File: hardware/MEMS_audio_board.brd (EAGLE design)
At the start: 43.2 x 25.4 mm, 20 parts, among them J1 SJ-2524-SMT, J2 USBSMD, U1 LMV793MF, U2 MIC5365-3.3YD5

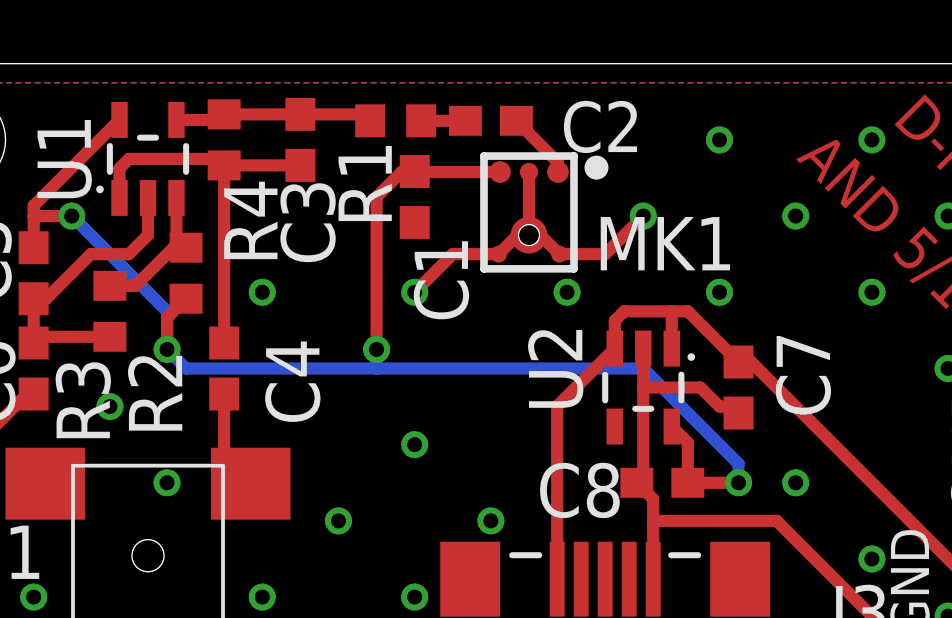
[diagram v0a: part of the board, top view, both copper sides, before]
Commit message: corrected flipped mic layout
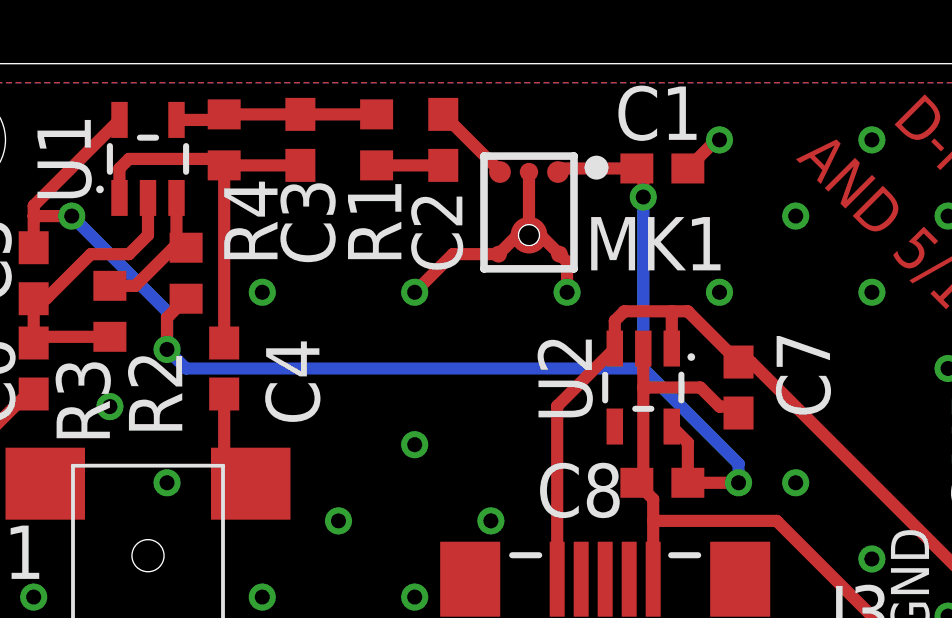
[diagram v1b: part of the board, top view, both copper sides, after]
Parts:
- moved C1 8.31 mm to (26.0, 21.9), turned to 0 degrees
- moved C2 1.71 mm to (18.7, 22.9), turned to 270 degrees
- moved R1 0.90 mm to (16.5, 22.9), turned to 90 degrees
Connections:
- net +3V3: now also MK1.P4; no longer MK1.4
- net GND: now also MK1.P2, MK1.P3, MK1.P5, MK1.P6; no longer MK1.2, MK1.3, MK1.5, MK1.6
- net OUT_DC: now also MK1.P1; no longer MK1.1
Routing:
- net +3V3: track 49.7 -> 48.9 mm
- net OUT_AC: track 1.47 -> 2.22 mm
- net GND: track 46.4 -> 45.9 mm, vias 31 -> 30
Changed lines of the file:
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@@
 <setting verticaltext="up"/>
 </settings>
-<grid distance="0.1" unitdist="inch" unit="inch" style="lines" multiple="1" display="yes" altdistance="0.025" altunitdist="inch" altunit="inch"/>
+<grid distance="0.1" unitdist="inch" unit="inch" style="lines" multiple="1" display="yes" altdistance="0.0125" altunitdist="inch" altunit="inch"/>
 <layers>
 <layer number="1" name="Top" color="4" fill="1" visible="yes" active="yes"/>
@@
 </element>
 <element name="MK1" library="Audio_Board_Parts" package="SPU0410LR5H-QB" value="SPU0410LR5H-QB" x="21.59" y="19.685" smashed="yes">
-<attribute name="NAME" x="23.765" y="18.51" size="1.778" layer="25" font="vector" ratio="20"/>
+<attribute name="NAME" x="23.4475" y="18.51" size="1.778" layer="25" font="vector" ratio="20"/>
 </element>
 <element name="U1" library="Audio_Board_Parts" package="SOT23-5" value="LMV793MF" x="8.89" y="22.225" smashed="yes">
@@
 </element>
 <element name="U2" library="Audio_Board_Parts" package="SOT23-5" value="MIC5365-3.3YD5" x="25.4" y="14.605" smashed="yes" rot="R180">
-<attribute name="NAME" x="21.59" y="15.24" size="1.778" layer="25" font="vector" ratio="20" rot="R270" align="bottom-center"/>
+<attribute name="NAME" x="21.9075" y="14.9225" size="1.778" layer="25" font="vector" ratio="20" rot="R270" align="bottom-center"/>
 </element>
 <element name="J1" library="Audio_Board_Parts" package="SJ-2524-SMT" value="SJ-2524-SMT" x="8.89" y="0" smashed="yes" rot="R90">
 <attribute name="NAME" x="4.445" y="8.225" size="1.778" layer="25" font="vector" ratio="20" align="bottom-center"/>
 </element>
-<element name="C1" library="rcl" package="C0603" value="100 nF" x="17.78" y="20.955" smashed="yes" rot="R270">
-<attribute name="NAME" x="17.78" y="19.685" size="1.778" layer="25" font="vector" ratio="20" rot="R270"/>
-</element>
-<element name="C2" library="rcl" package="C0603" value="4.7 uF" x="20.32" y="23.495" smashed="yes" rot="R180">
-<attribute name="NAME" x="25.4" y="24.13" size="1.6764" layer="25" font="vector" ratio="20" rot="R180"/>
-</element>
-<element name="R1" library="rcl" package="R0603" value="1.5 k" x="17.145" y="23.495" smashed="yes" rot="R180">
-<attribute name="NAME" x="15.24" y="22.86" size="1.778" layer="25" font="vector" ratio="20" rot="R270"/>
+<element name="C1" library="rcl" package="C0603" value="100 nF" x="26.035" y="21.9075" smashed="yes">
+<attribute name="NAME" x="24.4475" y="22.86" size="1.778" layer="25" font="vector" ratio="20"/>
+</element>
+<element name="C2" library="rcl" package="C0603" value="4.7 uF" x="18.7325" y="22.86" smashed="yes" rot="R270">
+<attribute name="NAME" x="19.3675" y="18.415" size="1.6764" layer="25" font="vector" ratio="20" rot="R90"/>
+</element>
+<element name="R1" library="rcl" package="R0603" value="1.5 k" x="16.51" y="22.86" smashed="yes" rot="R90">
+<attribute name="NAME" x="15.5575" y="21.59" size="1.778" layer="25" font="vector" ratio="20" rot="R270"/>
 </element>
 <element name="R2" library="rcl" package="R0603" value="10 k" x="10.16" y="18.415" smashed="yes" rot="R270">
@@
 <signals>
 <signal name="GND">
-<contactref element="MK1" pad="3"/>
-<contactref element="MK1" pad="5"/>
-<contactref element="MK1" pad="6"/>
-<contactref element="MK1" pad="2"/>
+<contactref element="MK1" pad="P3"/>
+<contactref element="MK1" pad="P5"/>
+<contactref element="MK1" pad="P6"/>
+<contactref element="MK1" pad="P2"/>
 <contactref element="C1" pad="2"/>
 <contactref element="R3" pad="1"/>
@@
 <via x="33.02" y="8.89" extent="1-16" drill="0.5"/>
 <via x="35.56" y="6.985" extent="1-16" drill="0.5"/>
-<via x="25.4" y="20.32" extent="1-16" drill="0.5"/>
 <polygon width="0.254" layer="1" spacing="1.4224" isolate="0.3048">
 <vertex x="0.635" y="24.765"/>
@@
 <vertex x="0.635" y="0.635"/>
 </polygon>
-<wire x1="21.971" y1="19.685" x2="22.605" y2="19.051" width="0.4064" layer="1"/>
 <wire x1="20.575" y1="19.051" x2="21.209" y2="19.685" width="0.4064" layer="1"/>
 <wire x1="21.209" y1="19.685" x2="21.59" y2="19.685" width="0.4064" layer="1"/>
 <wire x1="17.78" y1="17.78" x2="19.051" y2="19.051" width="0.4064" layer="1"/>
 <wire x1="19.051" y1="19.051" x2="20.575" y2="19.051" width="0.4064" layer="1"/>
-<wire x1="25.4" y1="20.32" x2="24.131" y2="19.051" width="0.4064" layer="1"/>
-<wire x1="24.131" y1="19.051" x2="22.605" y2="19.051" width="0.4064" layer="1"/>
 <wire x1="29.845" y1="10.16" x2="25.73" y2="10.16" width="0.4064" layer="1"/>
 <via x="5.08" y="7.62" extent="1-16" drill="0.5"/>
 <via x="9.525" y="11.43" extent="1-16" drill="0.5"/>
+<wire x1="27.94" y1="22.86" x2="27.8375" y2="22.86" width="0.4064" layer="1"/>
+<wire x1="27.8375" y1="22.86" x2="26.885" y2="21.9075" width="0.4064" layer="1"/>
+<wire x1="21.971" y1="19.685" x2="22.605" y2="19.051" width="0.4064" layer="1"/>
+<wire x1="22.86" y1="17.78" x2="22.86" y2="18.796" width="0.4064" layer="1"/>
+<wire x1="22.86" y1="18.796" x2="22.605" y2="19.051" width="0.4064" layer="1"/>
 </signal>
 <signal name="+3V3">
 <contactref element="C1" pad="1"/>
-<contactref element="MK1" pad="4"/>
+<contactref element="MK1" pad="P4"/>
 <contactref element="R2" pad="2"/>
 <contactref element="U1" pad="5"/>
@@
 <wire x1="26.35" y1="13.3049" x2="26.885" y2="12.7699" width="0.4064" layer="1"/>
 <wire x1="26.885" y1="12.7699" x2="26.885" y2="11.43" width="0.4064" layer="1"/>
-<wire x1="17.78" y1="21.805" x2="17.797" y2="21.788" width="0.4064" layer="1"/>
 <wire x1="5.08" y1="20.32" x2="5.08" y2="20.6651" width="0.4064" layer="1"/>
 <wire x1="5.08" y1="20.6651" x2="7.94" y2="23.5251" width="0.4064" layer="1"/>
 <via x="9.525" y="15.875" extent="1-16" drill="0.5"/>
 <wire x1="9.525" y1="15.875" x2="10.16" y2="15.24" width="0.4064" layer="16"/>
-<wire x1="10.16" y1="15.24" x2="16.51" y2="15.24" width="0.4064" layer="16"/>
-<wire x1="16.51" y1="15.24" x2="25.4" y2="15.24" width="0.4064" layer="16"/>
+<wire x1="10.16" y1="15.24" x2="25.4" y2="15.24" width="0.4064" layer="16"/>
 <wire x1="25.4" y1="15.24" x2="28.575" y2="12.065" width="0.4064" layer="16"/>
 <wire x1="28.575" y1="12.065" x2="28.575" y2="11.43" width="0.4064" layer="16"/>
@@
 <wire x1="10.16" y1="17.565" x2="9.525" y2="16.93" width="0.4064" layer="1"/>
 <wire x1="9.525" y1="16.93" x2="9.525" y2="15.875" width="0.4064" layer="1"/>
-<via x="16.51" y="15.875" extent="1-16" drill="0.5"/>
-<wire x1="16.51" y1="15.875" x2="16.51" y2="15.24" width="0.4064" layer="16"/>
-<wire x1="17.797" y1="21.788" x2="20.624" y2="21.788" width="0.4064" layer="1"/>
-<wire x1="16.51" y1="15.875" x2="16.51" y2="20.955" width="0.4064" layer="1"/>
-<wire x1="16.51" y1="20.955" x2="17.36" y2="21.805" width="0.4064" layer="1"/>
-<wire x1="17.36" y1="21.805" x2="17.78" y2="21.805" width="0.4064" layer="1"/>
+<wire x1="22.556" y1="21.788" x2="22.6755" y2="21.9075" width="0.4064" layer="1"/>
+<wire x1="22.6755" y1="21.9075" x2="25.185" y2="21.9075" width="0.4064" layer="1"/>
+<wire x1="25.4" y1="15.24" x2="25.4" y2="20.955" width="0.4064" layer="16"/>
+<via x="25.4" y="20.955" extent="1-16" drill="0.5"/>
+<wire x1="25.4" y1="20.955" x2="25.4" y2="21.6925" width="0.4064" layer="1"/>
+<wire x1="25.4" y1="21.6925" x2="25.185" y2="21.9075" width="0.4064" layer="1"/>
 </signal>
 <signal name="OUT_DC">
-<contactref element="MK1" pad="1"/>
+<contactref element="MK1" pad="P1"/>
 <contactref element="C2" pad="1"/>
-<wire x1="22.556" y1="21.788" x2="22.556" y2="22.109" width="0.4064" layer="1"/>
-<wire x1="22.556" y1="22.109" x2="21.17" y2="23.495" width="0.4064" layer="1"/>
+<wire x1="18.7325" y1="23.71" x2="20.624" y2="21.8185" width="0.4064" layer="1"/>
+<wire x1="20.624" y1="21.8185" x2="20.624" y2="21.788" width="0.4064" layer="1"/>
 </signal>
 <signal name="OUT_AC">
 <contactref element="C2" pad="2"/>
 <contactref element="R1" pad="1"/>
-<wire x1="19.47" y1="23.495" x2="17.995" y2="23.495" width="0.4064" layer="1"/>
+<wire x1="16.51" y1="22.01" x2="18.7325" y2="22.01" width="0.4064" layer="1"/>
 </signal>
 <signal name="V_BIAS">
@@
 <wire x1="11.43" y1="23.71" x2="11.2451" y2="23.5251" width="0.4064" layer="1"/>
 <wire x1="11.2451" y1="23.5251" x2="9.84" y2="23.5251" width="0.4064" layer="1"/>
-<wire x1="13.97" y1="23.71" x2="16.08" y2="23.71" width="0.4064" layer="1"/>
-<wire x1="16.08" y1="23.71" x2="16.295" y2="23.495" width="0.4064" layer="1"/>
+<wire x1="13.97" y1="23.71" x2="16.51" y2="23.71" width="0.4064" layer="1"/>
 </signal>
 <signal name="N$4">
